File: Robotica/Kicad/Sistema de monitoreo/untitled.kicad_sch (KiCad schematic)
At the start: 1 part, among them J1 Conn_01x03_Pin

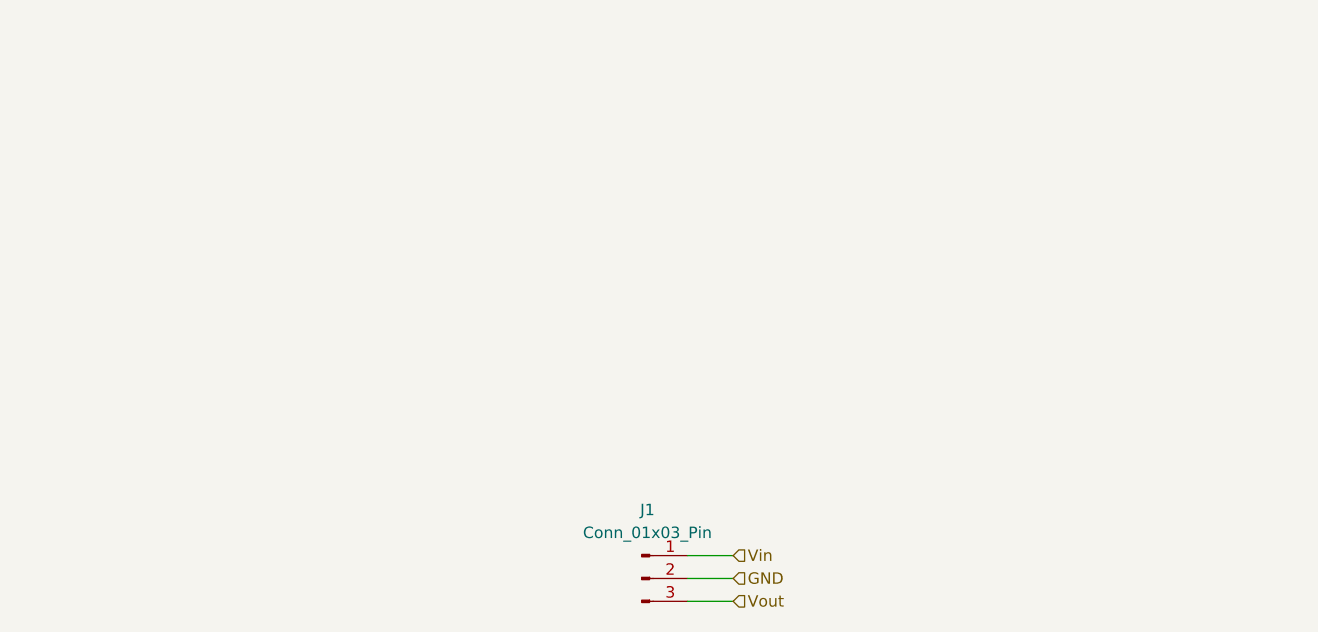
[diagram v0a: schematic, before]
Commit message: Organizacion de esquematicos de robotica
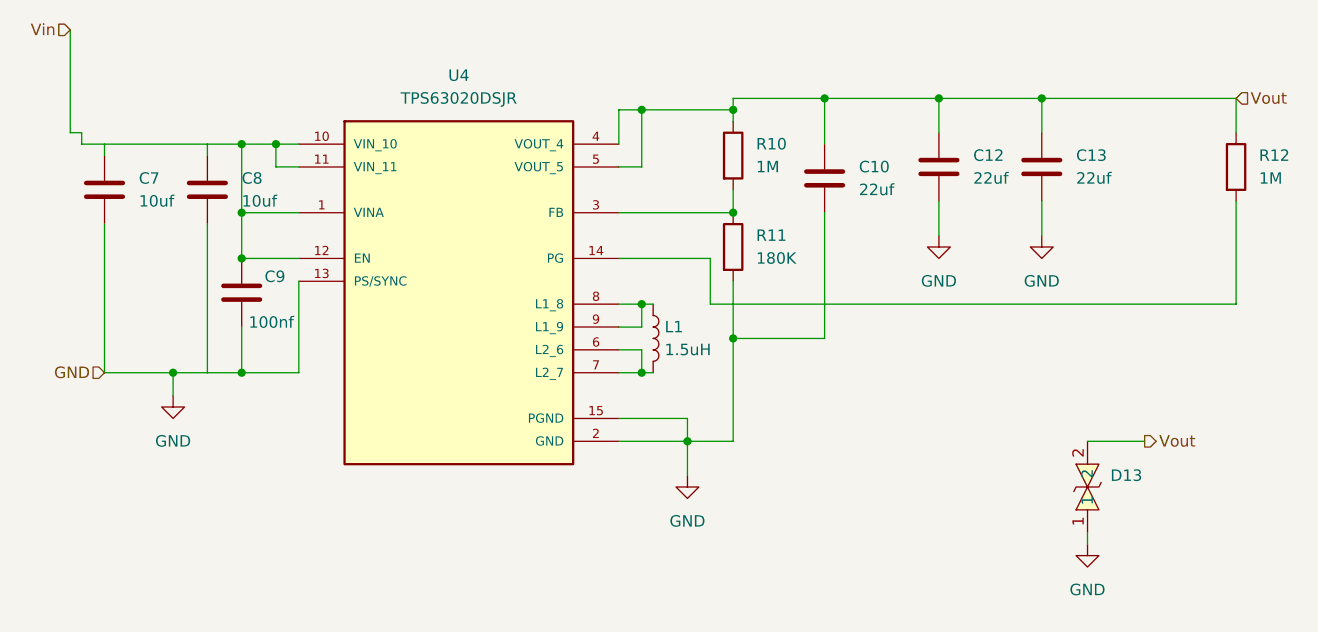
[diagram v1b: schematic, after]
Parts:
- removed J1: Conn_01x03_Pin, Connector_PinHeader_2.54mm:PinHeader_1x03_P2.54mm_Vertical, symbol Connector:Conn_01x03_Pin
- added C10, C12, C13: 22uf, Capacitor_SMD:C_0805_2012Metric_Pad1.18x1.45mm_HandSolder, symbol Device:C
- added C7, C8: 10uf, Capacitor_SMD:C_0805_2012Metric_Pad1.18x1.45mm_HandSolder, symbol Device:C
- added C9: 100nf, Capacitor_SMD:C_0805_2012Metric_Pad1.18x1.45mm_HandSolder, symbol Device:C
- added D13: ESD5B5.0ST1G, Diode_SMD:D_SOD-523, symbol ESD5B5.0ST1G:ESD5B5.0ST1G
- added L1: 1.5uH, L_APV_APH0630, symbol Device:L
- added R10, R12: 1M, Resistor_SMD:R_0805_2012Metric_Pad1.20x1.40mm_HandSolder, symbol Device:R
- added R11: 180K, Resistor_SMD:R_0805_2012Metric_Pad1.20x1.40mm_HandSolder, symbol Device:R
- added U4: TPS63020DSJR, tps63020:TPS63020DSJR, symbol TPS63020DSJR:TPS63020DSJR
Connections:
- net GND: now also C10.2, C12.2, C13.2, C7.2, C8.2, C9.2, D13.1, R11.2, U4.13 (PS/SYNC), U4.15 (PGND), U4.2 (GND)
- net Vin: now also C8.1, C9.1, U4.1 (VINA), U4.10 (VIN_10), U4.11 (VIN_11), U4.12 (EN)
- net Vout: now also C10.1, C12.1, C13.1, D13.2, R10.1, R12.1, U4.4 (VOUT_4), U4.5 (VOUT_5)
- new net: R12.2, U4.14 (PG)
- new net: R10.2, R11.1, U4.3 (FB)
- new net: L1.2, U4.6 (L2_6), U4.7 (L2_7)
- new net: L1.1, U4.8 (L1_8), U4.9 (L1_9)
